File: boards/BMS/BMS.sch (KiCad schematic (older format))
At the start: 55 parts, among them IC1 ATMEGA16M1, J1 Mounting_Hole_4-40, J2 Mounting_Hole_4-40, J3 Mounting_Hole_4-40, J4 Ultrafit_4, J5 Mounting_Hole_4-40, K1 G5Q-1A, P1 CONN_02X03, Q1 2N7002, Q2 NMOS_GSD_30V, Q3 NMOS_GSD_30V, U1 micro-match12pin, U2 CAN_Transceiver, U3 TPS561201, U4 SN74LVC1G17, Y1 Crystal_SMD

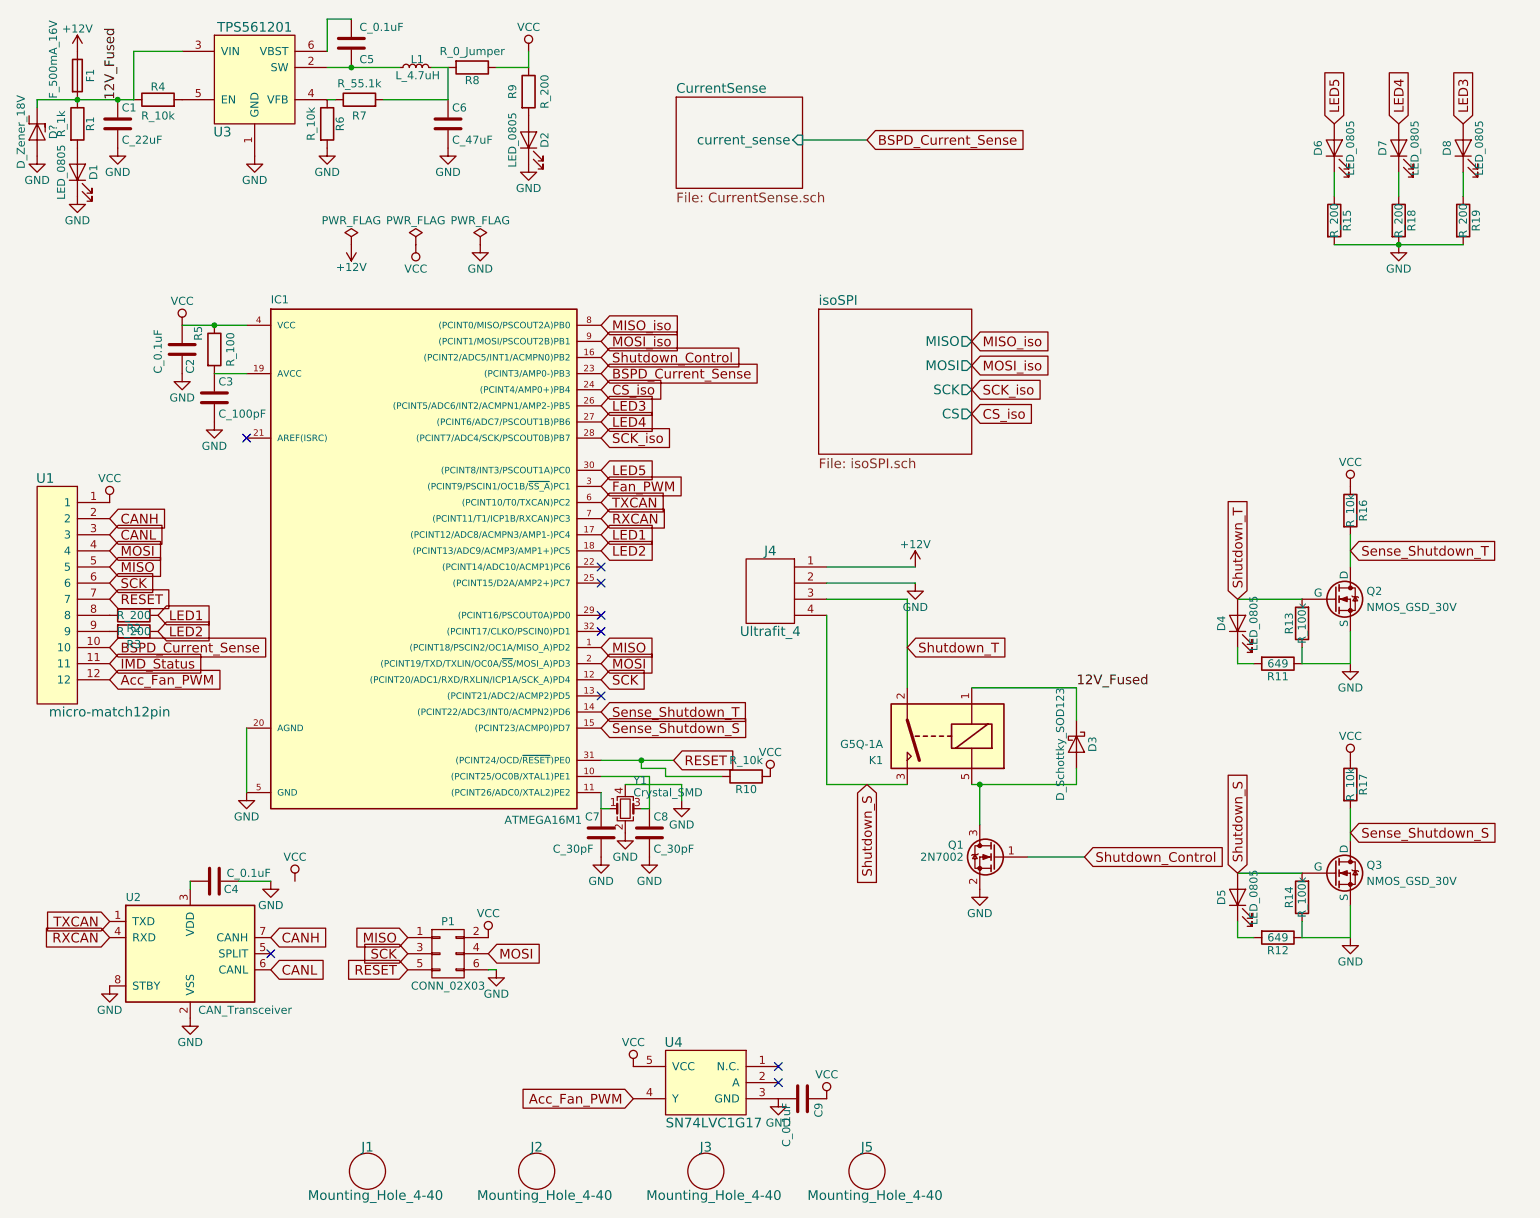
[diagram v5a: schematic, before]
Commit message: BMS debugging, slave components added
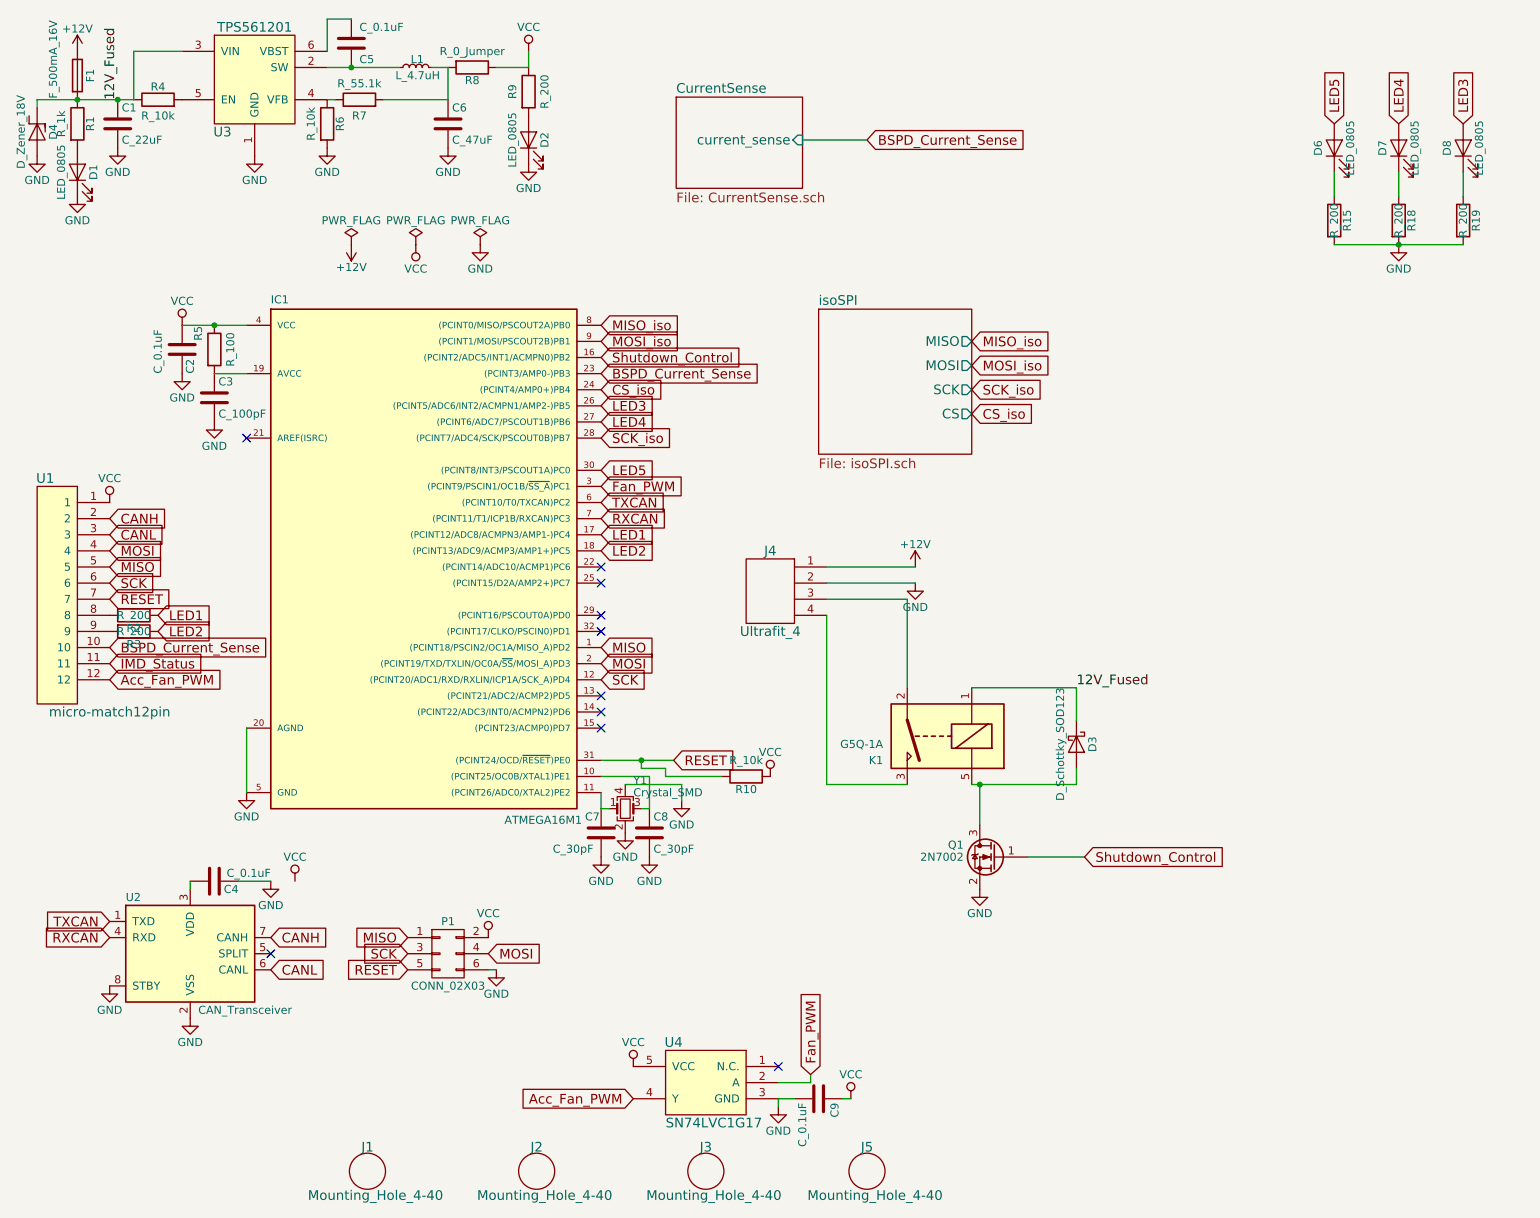
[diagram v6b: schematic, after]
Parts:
- removed D4, D5: LED_0805, LEDs:LED_0805, symbol LED_0805
- removed Q2, Q3: NMOS_GSD_30V, TO_SOT_Packages_SMD:SOT-23, symbol NMOS_GSD_30V
- removed R11, R12: 649, symbol R
- removed R13, R14: R_100k, Resistors_SMD:R_0805, symbol R_100k
- removed R16, R17: R_10k, Resistors_SMD:R_0805, symbol R_10k
- gave numbers to parts that had none: 1
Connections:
- net Fan_PWM: now also U4.2 (A)
- net Sense_Shutdown_S: no longer names the net of IC1.15 ((PCINT23/ACMP0)PD7)
- net Sense_Shutdown_T: no longer names the net of IC1.14 ((PCINT22/ADC3/INT0/ACMPN2)PD6)
- net Shutdown_S: no longer names the net of J4.4, K1.3
- net Shutdown_T: no longer names the net of J4.3, K1.2
- no-connect marks 9 -> 10
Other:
- moved on the sheet: C9

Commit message: Progress
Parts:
- removed K1: G5Q-1A, Relays_THT:Relay_SPST-NO_OMRON-G5Q, symbol G5Q-1A
- removed R8: R_0_Jumper, Resistors_SMD:R_2512, symbol R_0_Jumper
- added K1: G5Q-1A4-DC5-5V, footprints:Relay_SPST_OMRON-G5Q-1A4_OEM, symbol G5Q-1A4-DC5-5V
- C1: footprint Capacitors_SMD:C_1206 -> footprints:C_1206_OEM
- C2, C3, C4, C5, C6, C7, C8, C9: footprint Capacitors_SMD:C_0805 -> footprints:C_0805_OEM
- D1, D2, D6, D7, D8: footprint LEDs:LED_0805 -> footprints:LED_0805_OEM
- D3: footprint Diodes_SMD:D_SOD-123 -> footprints:D_SOD-123W_OEM
- IC1: footprint Housings_QFP:TQFP-32_7x7mm_Pitch0.8mm -> footprints:TQFP-32_7x7mm_Pitch0.8mm
- Q1: footprint TO_SOT_Packages_SMD:SOT-23 -> footprints:SOT-23F
- R1, R15, R18, R19, R2, R3, R4, R5, R6, R7, R9: footprint Resistors_SMD:R_0805 -> footprints:R_0805_OEM
- R10: footprint Resistors_SMD:R_0805 -> footprints:D_0805_OEM
- U1: footprint (none) -> footprints:micromatch_female_ra_12
- U2: footprint Housings_SOIC:SOIC-8_3.9x4.9mm_Pitch1.27mm -> footprints:SOIC-8_3.9x4.9mm_Pitch1.27mm_OEM
- U3: footprint TO_SOT_Packages_SMD:SOT-23-6 -> footprints:SOT-23-6_OEM
- U4: footprint (none) -> footprints:SOT-23-5_OEM
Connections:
- net IMD_Status is gone; now on net Acc_Fan_PWM: U1.11
- net Acc_Fan_PWM: no longer U1.12
- net Shutdown_Control: now also U1.12
- net VCC: now also C6.1, D3.1 (K), L1.2, R7.2, K1.1
- net at J4.3: now also K1.2
- net at J4.4: now also K1.3
- net at D3.2 (A), Q1.3 (D): now also K1.5
- net 12V_Fused: no longer names the net of C1.1, D4.1 (K), F1.2, R1.1, R4.1, U3.3 (VIN)
- net 12V_Fused: no longer D3.1 (K)
- no-connect marks 10 -> 11
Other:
- moved on the sheet: Q1

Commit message: BMS: update file
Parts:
- added J8: Ultrafit_2, footprints:Ultrafit_2, symbol Ultrafit_2
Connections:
- net GND: now also J8.2
- net at IC1.22 ((PCINT14/ADC10/ACMP1)PC6): now also J8.1
- no-connect marks 11 -> 9
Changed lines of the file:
@@
 NoConn ~ 4050 4350
 NoConn ~ 4050 4150
-NoConn ~ 4050 4050
 NoConn ~ 1850 3250
 NoConn ~ 4050 4850
@@
 	1    0    0    -1
 $EndComp
-NoConn ~ 1250 1100
 Connection ~ 3100 950
 Wire Wire Line
@@
 Text GLabel 1000 4750 2    60   Input ~ 0
 Shutdown_Control
+$Comp
+L Ultrafit_2 J8
+U 1 1 5A6A8A5C
+P 4850 3450
+F 0 "J8" H 4850 3600 60  0000 C CNN
+F 1 "Ultrafit_2" H 4950 3250 60  0000 C CNN
+F 2 "footprints:Ultrafit_2" H 4750 3500 60  0001 C CNN
+F 3 "" H 4850 3600 60  0001 C CNN
+F 4 "https://www.digikey.com/product-detail/en/molex-llc/1722861102/WM11570-ND/5344267" H 4950 3700 60  0001 C CNN "PurchasingLink"
+F 5 "Digi-Key" H 5050 3800 60  0001 C CNN "MFN"
+F 6 "WM11570-ND" H 5150 3900 60  0001 C CNN "MPN"
+F 7 "Value" H 5250 4000 60  0001 C CNN "Package"
+	1    4850 3450
+	1    0    0    -1
+$EndComp
+$Comp
+L GND #PWR034
+U 1 1 5A6A8B59
+P 5100 3500
+F 0 "#PWR034" H 5100 3250 50  0001 C CNN
+F 1 "GND" H 5100 3350 50  0000 C CNN
+F 2 "" H 5100 3500 50  0001 C CNN
+F 3 "" H 5100 3500 50  0001 C CNN
+	1    5100 3500
+	1    0    0    -1
+$EndComp
+Wire Wire Line
+	4050 4050 4850 4050
+Wire Wire Line
+	4850 4050 4850 3800
+Wire Wire Line
+	4850 3800 5300 3800
+Wire Wire Line
+	5300 3800 5300 3400
+Wire Wire Line
+	5300 3400 5100 3400
 $EndSCHEMATC
